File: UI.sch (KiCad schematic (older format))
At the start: 36 parts, among them Q1 2N7002BK, Q2 BS250P

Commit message: Changed Membrane push buttons from zener to schottky diodes
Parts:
- removed D? (x4): SP3522-01UTG, 0603 diode, symbol OpenVent:SP3522-01UTG
- removed FB? (x4): BLA31BD121SN4D, F_Inductors:Murata_BLA31, symbol OpenVent:BLA31BD121SN4D
- added D15, D16: BAT54XYH, symbol OpenVent:BAT54XYH
- added R? (x4): 1K_0603_Chip_Resistor,_1%,_0.1W, symbol OpenVent:1K_0603_Chip_Resistor,_1%,_0.1W
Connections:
- wire segments 242 -> 235
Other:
- moved on the sheet: C?, JP?, LCD?, LS1, LS2, Q1, Q2, R35, R36, R49, R?, U?

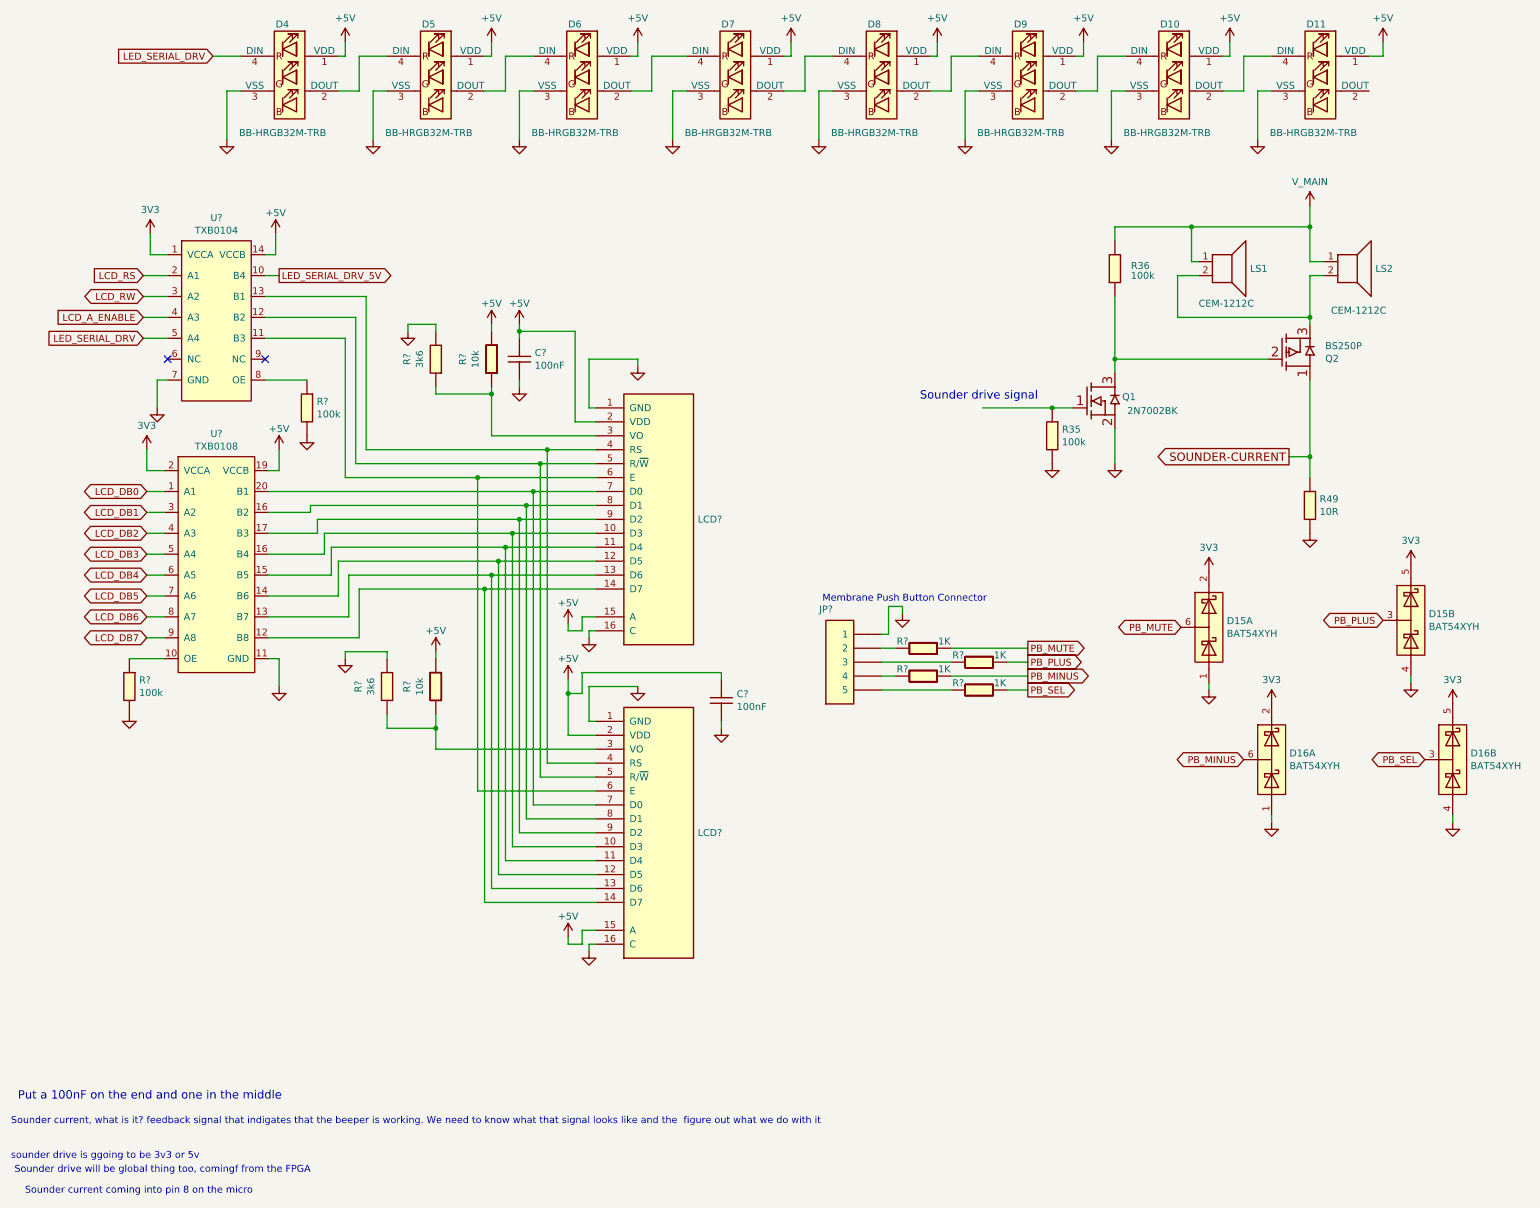
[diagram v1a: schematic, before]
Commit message: Header 2x5 for FPGA was added to JTAG sheet
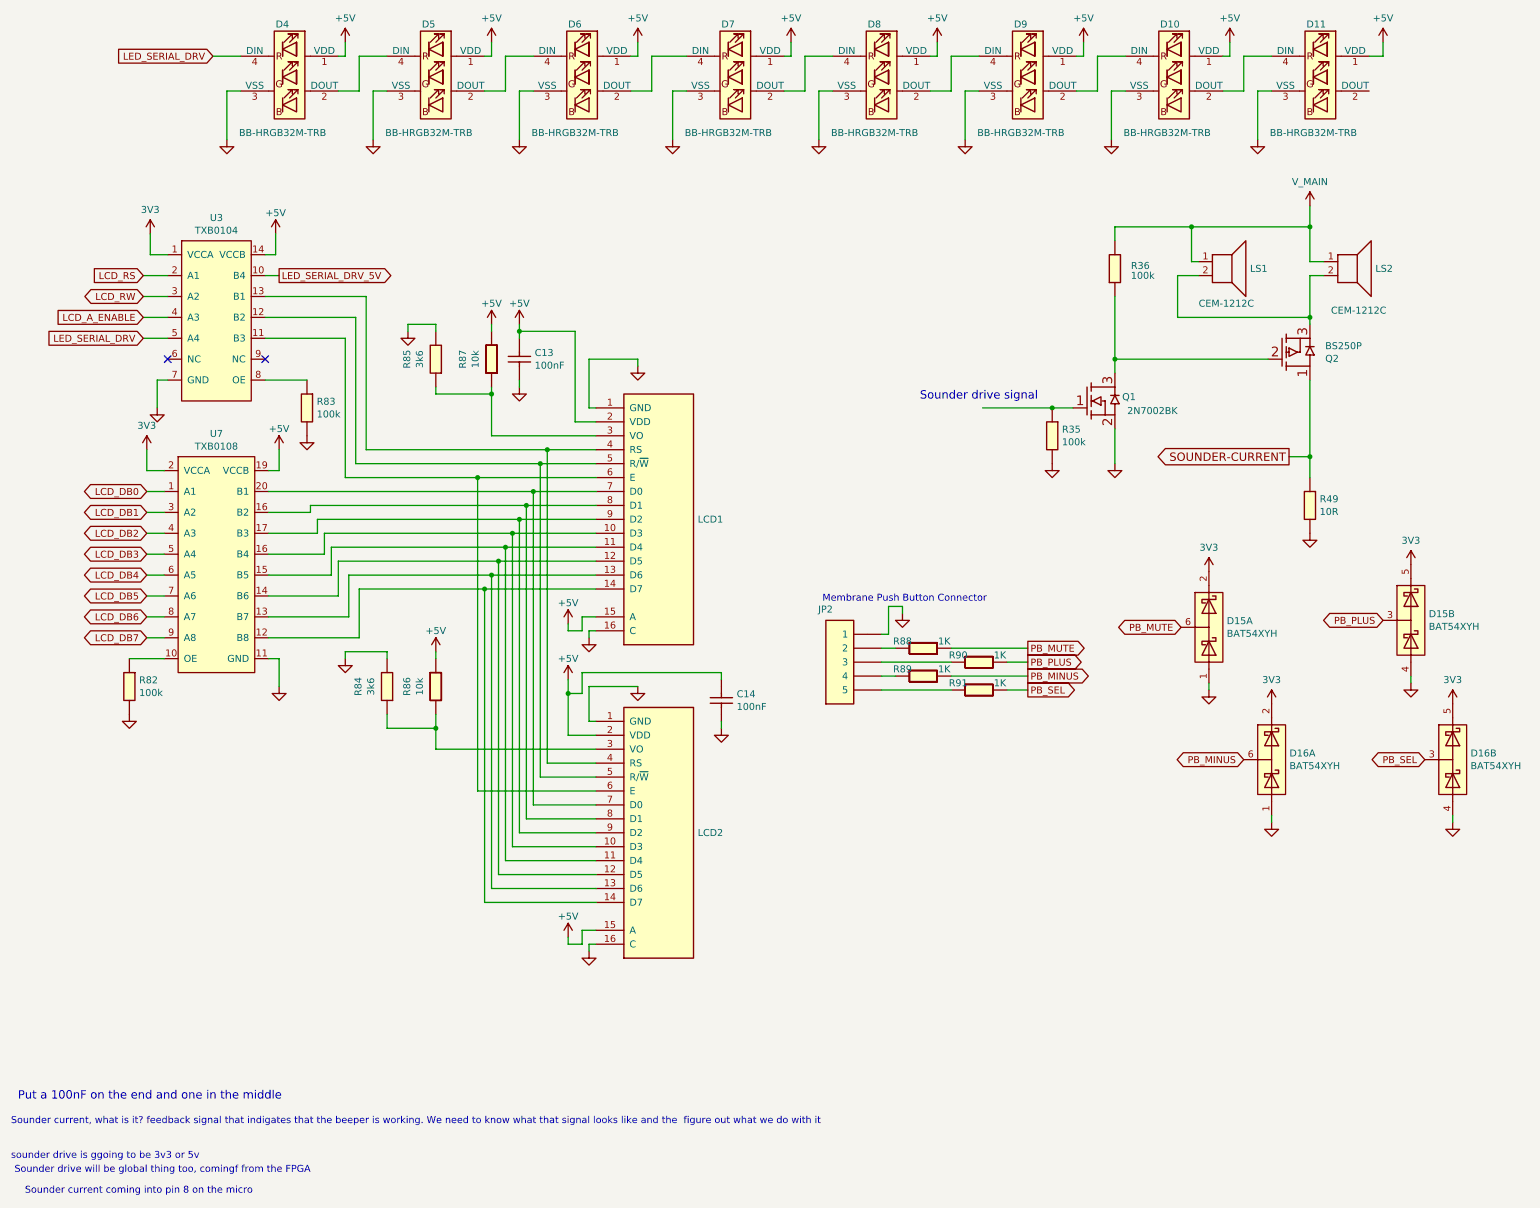
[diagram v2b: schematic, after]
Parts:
- gave numbers to parts that had none: 17

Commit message: Add 470 pF capacitor from U2 pin 5 to ground Add 100 nF cap to each LED, D4 to D11
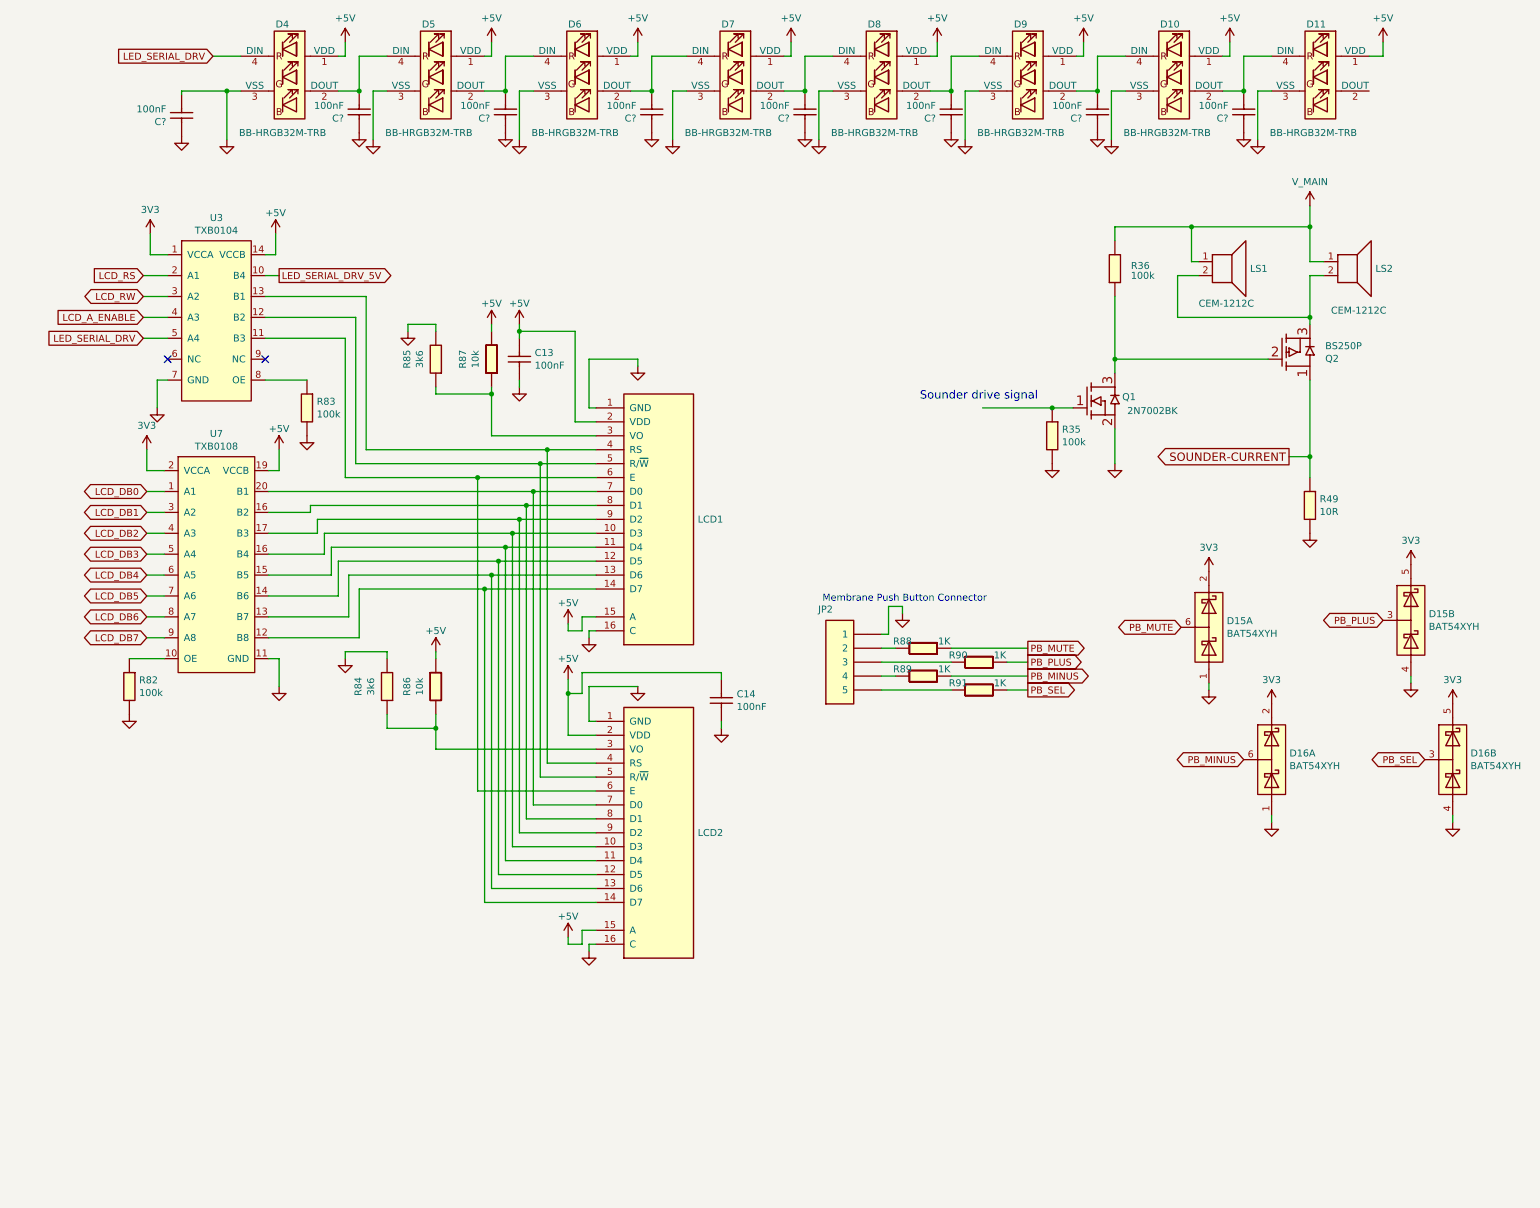
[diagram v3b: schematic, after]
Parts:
- added C? (x8): 100nF_0603_Ceramic_Capacitor,_10%,_X7R,_25V, symbol OpenVent:100nF_0603_Ceramic_Capacitor,_10%,_X7R,_25V
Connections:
- net GND: now also C?.1, C?.1, C?.1, C?.1, C?.1, C?.1, C?.1, C?.1, C?.2
- net at D8.2 (DOUT), D9.4 (DIN): now also C?.2
- net at D7.2 (DOUT), D8.4 (DIN): now also C?.2
- net at D10.4 (DIN), D9.2 (DOUT): now also C?.2
- net at D10.2 (DOUT), D11.4 (DIN): now also C?.2
- net at D6.2 (DOUT), D7.4 (DIN): now also C?.2
- net at D5.2 (DOUT), D6.4 (DIN): now also C?.2
- net at D4.2 (DOUT), D5.4 (DIN): now also C?.2
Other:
- note removed: "Put a 100nF on the end and one in the middle\n"
- note removed: "Sounder current coming into pin 8 on the micro"
- note removed: "Sounder current, what is it? feedback signal that indigates that the beeper is working. We need to know what that signal looks like and the figure out what we do with it"
- note removed: "Sounder drive will be global thing too, comingf from the FPGA"
- note removed: "sounder drive is ggoing to be 3v3 or 5v"
